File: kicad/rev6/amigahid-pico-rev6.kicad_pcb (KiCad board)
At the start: 2 copper layers, 100 x 80 mm, 115 parts, among them J1 A500 KBD OUT, J10 PS/2 KBD OUT, J11 DIN5 KBD IN, J12 PS/2 KBD IN, J13 USB-C AUX 5V, J2 DEBUG UART+SWD, J3 OLED I2C, J4 USB-A HOST, J7 SPARE GP28, J8 A500 KBD IN, J9 DIN5 KBD OUT, P1 DE9 MALE PORT 1, P2 DE9 MALE PORT 2, Q1 BSS138, Q10 BSS138, Q11 BSS138, Q12 BSS138, Q13 BSS138, Q14 BSS138, Q15 BSS138, Q16 BSS138, Q17 BSS138, Q18 BSS138, Q19 BSS138, Q2 BSS138, Q3 BSS138, Q4 BSS138, Q5 BSS138, Q6 BSS138, Q7 BSS138, Q8 BSS138, Q9 BSS138, U1 PicoW, U2 USBLC6-2SC6

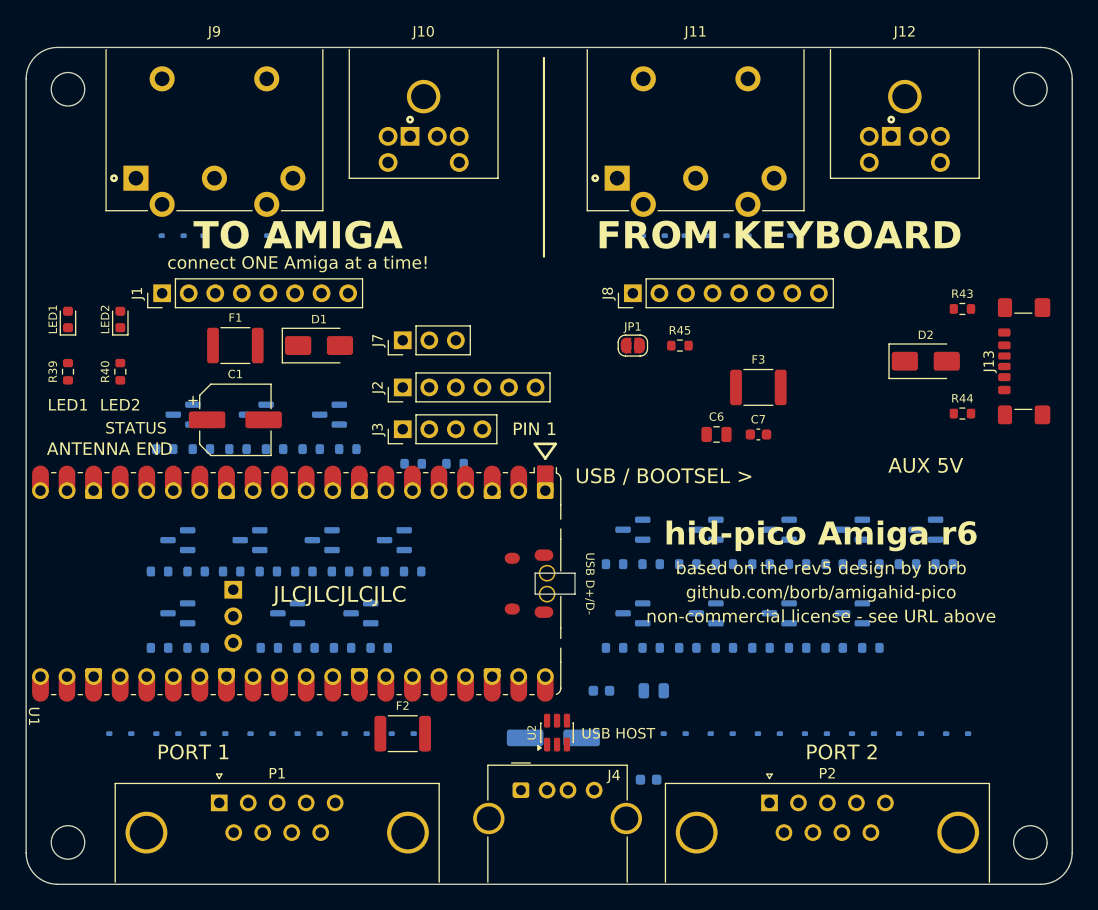
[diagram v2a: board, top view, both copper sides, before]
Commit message: kicad: route rev6 board
Copper for the whole board: 1524 track segments and 714 vias, 3.2 m of
copper, plus GND pours on both layers (69% / 68% coverage) with 400-odd
stitching vias on a 4 mm grid.  Power runs at 1.0 mm on its own netclass,
signals at 0.25 mm, +3V3 at 0.5 mm; the pours use thermal spokes on
through-hole pads and solid connections on SMD.

The shifter field had to be rearranged to make the board routable at all.
As drawn at M2 all four BSS138 groups sat between U1's two pad rows, and
the pull-ups lay flat at 1.6 mm pad pitch, which left 0.84-1.06 mm gaps -
about 0.4 mm of usable lane once clearance comes off, so almost nothing
could cross a pull-up row and the channels had to detour round the ends.
So:

  - every pull-up stands on end (90 deg), which cuts its width across the
    row from 2.4 mm to 0.95 mm and opens the gaps to ~2.5 mm.  All of
    them face the same way, channel pad toward its FET, rail pad away,
    so the SYS5V rail no longer runs along a row of channel pads.
  - each FET row moved 0.8-1.3 mm off its pull-ups, turning 0.63 mm dead
    lanes into 1.4-1.9 mm ones.
  - the b1/b2/b3 groups of both ports moved south of the module, into the
    band that only held the ESD clamps, next to the connector pins they
    serve.  The clamps moved south to make room.
  - U2 turned 180 deg: its VBUS pin was boxed in between the two USB data
    pins with 0.35 mm either side and a ground pad due south.

The USB pair is laid by hand.  Both taps sit on the edge of the milled
window, so each run starts 0.43 mm clear of it inside its castellated
pad; usb_dp goes west round the window and threads the 0.94 mm gap
between U1's bottom castellations 39 and 40, usb_dm runs down the east
side with a 1.5 mm jog to match length.  24.4 mm and 20.7 mm, 3.7 mm
apart.  J13's USB-C VBUS pins are hand laid too: 0.29 mm of gap to the
CC pads means they leave on a 0.6 mm neck before widening.

tools/check_rev6_pcb.py: all 31 assertions pass.
tools/check_rev6_netlist.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
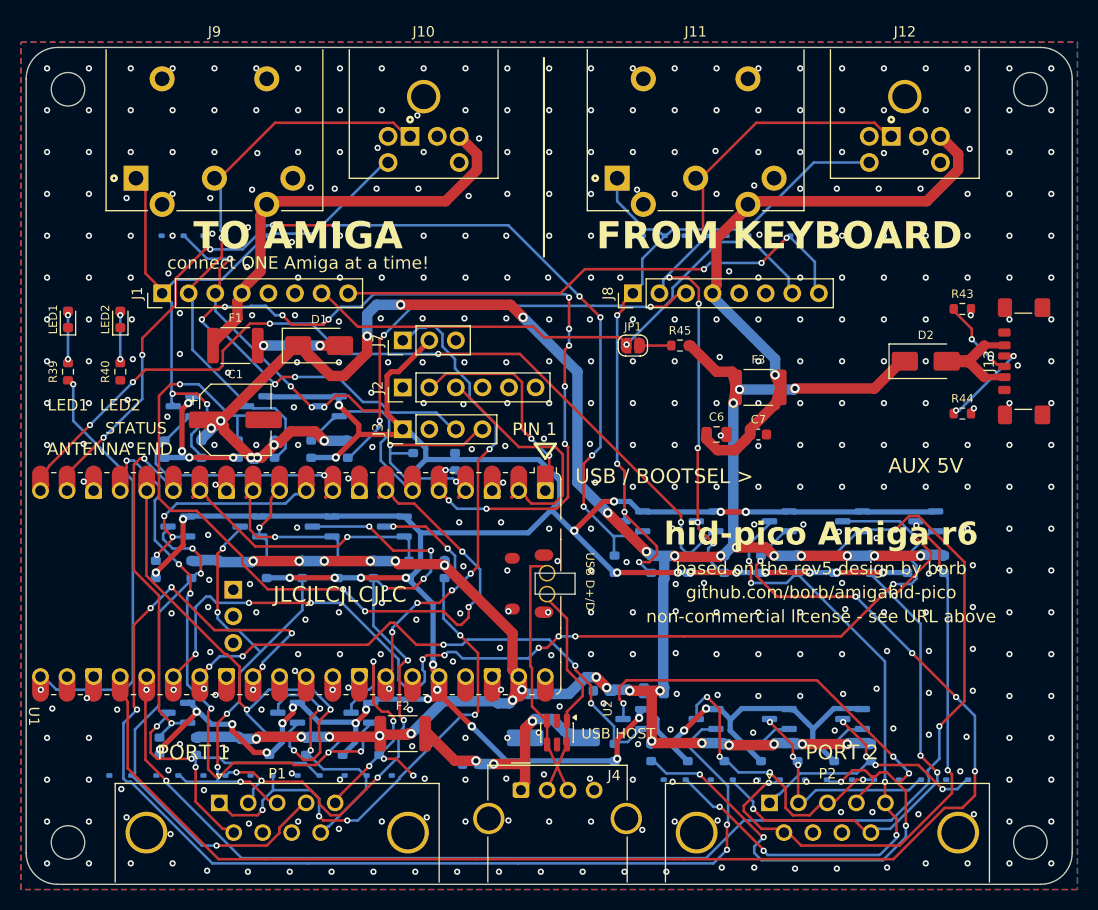
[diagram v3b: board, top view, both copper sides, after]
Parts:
- moved C5 17.1 mm to (42.5, 68.5)
- moved Q16 10.1 mm to (58.0, 64.2)
- moved Q17 10.1 mm to (65.0, 64.2)
- moved Q18 10.1 mm to (72.0, 64.2)
- moved Q19 10.1 mm to (79.0, 64.2)
- moved R31 10.0 mm to (56.2, 67.4), turned to 90 degrees
- moved R32 10.0 mm to (59.8, 67.4), turned to -90 degrees
- moved R33 10.0 mm to (63.2, 67.4), turned to 90 degrees
- moved R34 10.0 mm to (66.8, 67.4), turned to -90 degrees
- moved R35 10.0 mm to (70.2, 67.4), turned to 90 degrees
- moved R36 10.0 mm to (73.8, 67.4), turned to -90 degrees
- moved R37 10.0 mm to (77.2, 67.4), turned to 90 degrees
- moved R38 10.0 mm to (80.8, 67.4), turned to -90 degrees
- moved Q10 9.50 mm to (32.0, 63.6)
- moved Q8 9.50 mm to (14.5, 63.6)
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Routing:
- net +3V3: track 0.00 -> 321.5 mm, vias 0 -> 40
- net /SYS5V: track 0.00 -> 283.2 mm, vias 0 -> 45
- net /cont2_b3_lo: track 0.00 -> 135.1 mm, vias 0 -> 5
- net /cont2_b2_lo: track 0.00 -> 130.0 mm, vias 0 -> 4
- net /cont2_vq_lo: track 0.00 -> 118.4 mm, vias 0 -> 8
- net /i2c_scl: track 0.00 -> 104.0 mm, vias 0 -> 14
- net /kbin_clk_lo: track 0.00 -> 98.8 mm, vias 0 -> 9
- net /cont2_b1_lo: track 0.00 -> 96.1 mm, vias 0 -> 10
- net /kbin_dat_lo: track 0.00 -> 85.7 mm, vias 0 -> 5
- net /cont2_hq: track 0.00 -> 84.5 mm, vias 0 -> 7
- net /kbdata_lo: track 0.00 -> 79.7 mm, vias 0 -> 5
- net /kbreset: track 0.00 -> 75.2 mm, vias 0 -> 7
- net /kbin_clk: track 0.00 -> 68.6 mm, vias 0 -> 4
- net /kbin_dat: track 0.00 -> 67.1 mm, vias 0 -> 6
- net /cont2_b3: track 0.00 -> 64.7 mm, vias 0 -> 6
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- added copper zone on B.Cu, net GND
- added copper zone on F.Cu, net GND

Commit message: kicad: finish the rev6 copper
Pours re-laid with a 2.5 mm stitching grid (1028 ground vias, 69.3% /
68.8% coverage), thermal relief tightened to 0.15 mm gap / 0.4 mm spokes
so the through-hole ground pads keep two spokes, and the rail vias taken
down to 0.6/0.3 - at 0.8/0.4 a handful sat 0.475 mm from a 0603 pad's
copper where the copper-to-hole rule wants 0.5 mm.

The USB pair is re-laid to swap sides on the back layer just in front of
J4: U2 puts usb_dp on the west column and J4 on the east, so the pair has
to cross once, and doing it under the board keeps both runs clear of each
other.  usb_dp 24.7 mm, usb_dm 22.8 mm.

DRC is down to 2 starved thermals and 12 unconnected items; the detail is
in the commit thread.  Netlist checker 356/356, pcb checker 31/31.
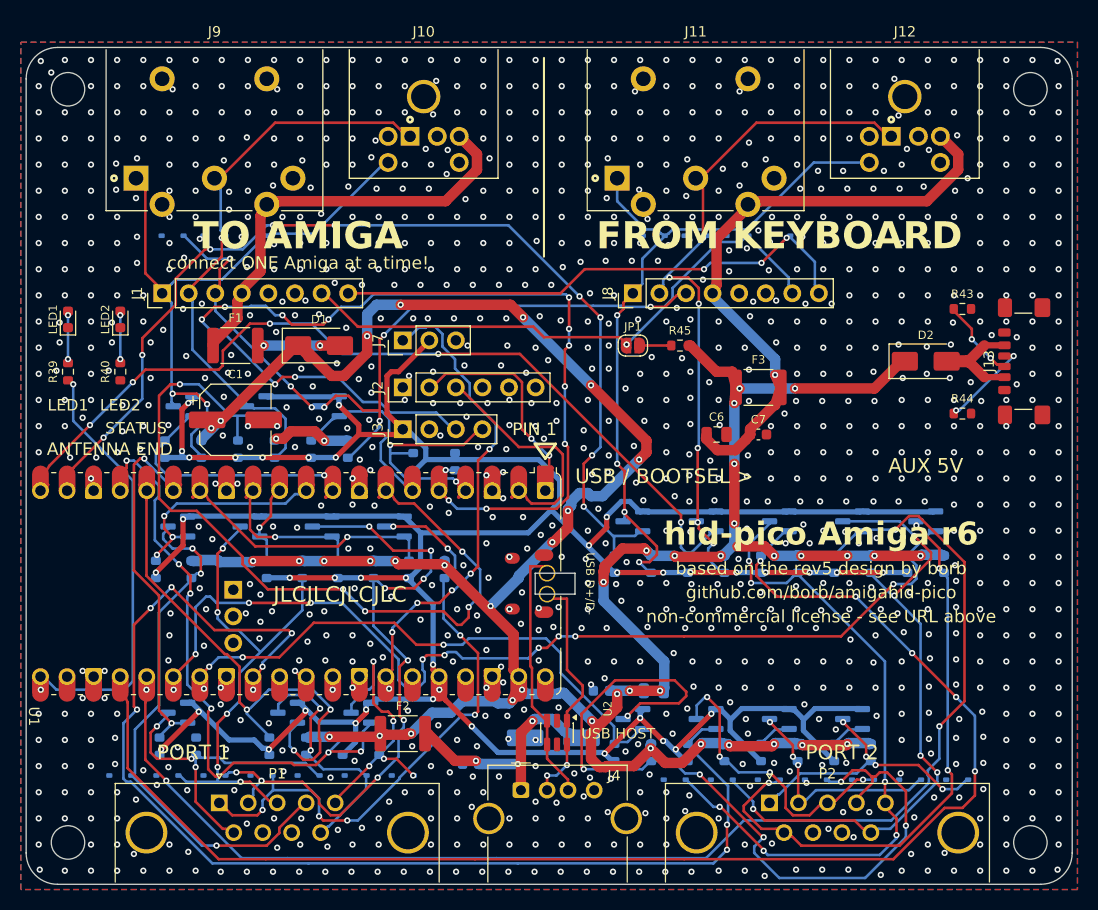
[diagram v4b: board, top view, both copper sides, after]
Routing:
- net /SYS5V: track 283.2 -> 292.5 mm, vias 45 -> 48
- net +3V3: track 321.5 -> 325.9 mm, vias 40 -> 39
- net /cont2_hq: track 84.5 -> 80.8 mm, vias 7 -> 6
- net /usb_dm: track 20.7 -> 22.8 mm, vias 0 -> 2
- net /cont2_hq_lo: vias 6 -> 4
- net GND: vias 426 -> 1028

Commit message: kicad: rf board keep-out, shifter designators and jlc-legal silk
Layout review fixes that touch no signal copper.  DRC is unchanged by this
commit: still the same 2 starved thermals on U1 pad 28 and the same 12
unconnected items, and no new violation of any other kind.

Outline
  - Cut the west edge back to x = 8.5 mm between y = 43.71 and 58.81 with R1
    inner fillets.  Raspberry Pi's own Pico W footprint carries a "Board Keep
    Out Suggestion RF" rectangle on Edge.Cuts reaching 8.5 mm inboard of the
    antenna end: the carrier is meant to be cut away under the antenna, not
    merely kept free of copper, and the board only overhung it by 1 mm.  The
    strip lies between the module's two pad rows and inside the antenna
    keep-out, so it was already empty - nothing was moved to make room, both
    pad rows keep full support, and copper-to-edge is unaffected.
  - Dropped 9 GND stitching vias that sat 0.31-0.42 mm from the M3 holes.
    Those holes are Edge.Cuts cutouts, so they are milled with profile
    tolerance rather than drilled; 0.3 mm is inside JLC's rule but is not much
    to hand a router bit, and these are redundant vias in a pour.

Connectors
  - Mini-DIN SH hole 2.40 -> 2.50 mm, in the footprint and both instances.
    2.40 leaves the Kycon KMDGX alternate's 2.30 mm locating boss only 0.10 mm
    diametral slack, which becomes a press fit once plating and hole tolerance
    come off; the Same Sky flat earth tab does not care.  The 3.20 mm pad still
    keeps a 0.35 mm ring.  Three stitching vias moved out of the way to hold
    the 0.5 mm hole-to-hole spacing.

Silkscreen
  - Turned on and placed all 78 hidden designators: Q1-Q19, R1-R38 and
    D10-D30, i.e. the whole bottom-side shifter and clamp field, which printed
    as an anonymous grid of SOT-23s and 0603s.  Bring-up probes those channels
    and the rework path is hand-soldering.
  - J9/J10/J11/J12 printed their designators at y = -1.5 mm, entirely off the
    board; they now sit in the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
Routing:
- net GND: track 0.00 -> 4.50 mm, vias 1028 -> 1021
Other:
- outline, holes or cut-outs redrawn

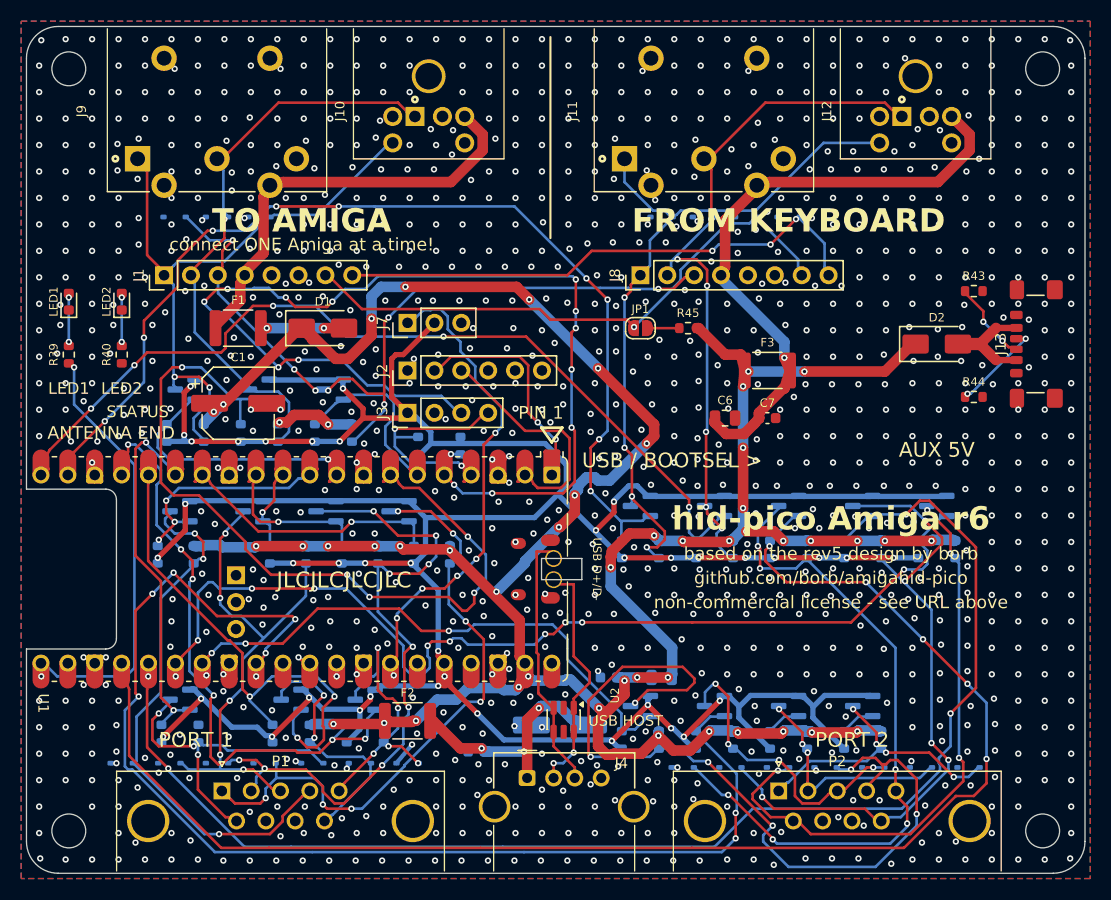
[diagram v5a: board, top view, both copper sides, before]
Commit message: kicad: thin the rev6 stitching via field
the board carried 1021 ground stitching vias on a 2.5 mm grid.  with
min_hole_clearance at 0.5 mm that is a pegboard: every corridor a signal needs is
fenced off by via holes, which is why eight nets were still open and four ESD clamps
were sitting on pour islands of their own.

the layout plan only asks for a tie about every 10 mm in open regions and the checker
only wants fifteen, so the field goes.  what is left are the vias that carry a stub -
clamp anchors and island ties - and the ties the stitcher then adds to keep the plane
one electrical island.  1021 vias down to 25.

no net changes: the same twelve items are unconnected before and after.
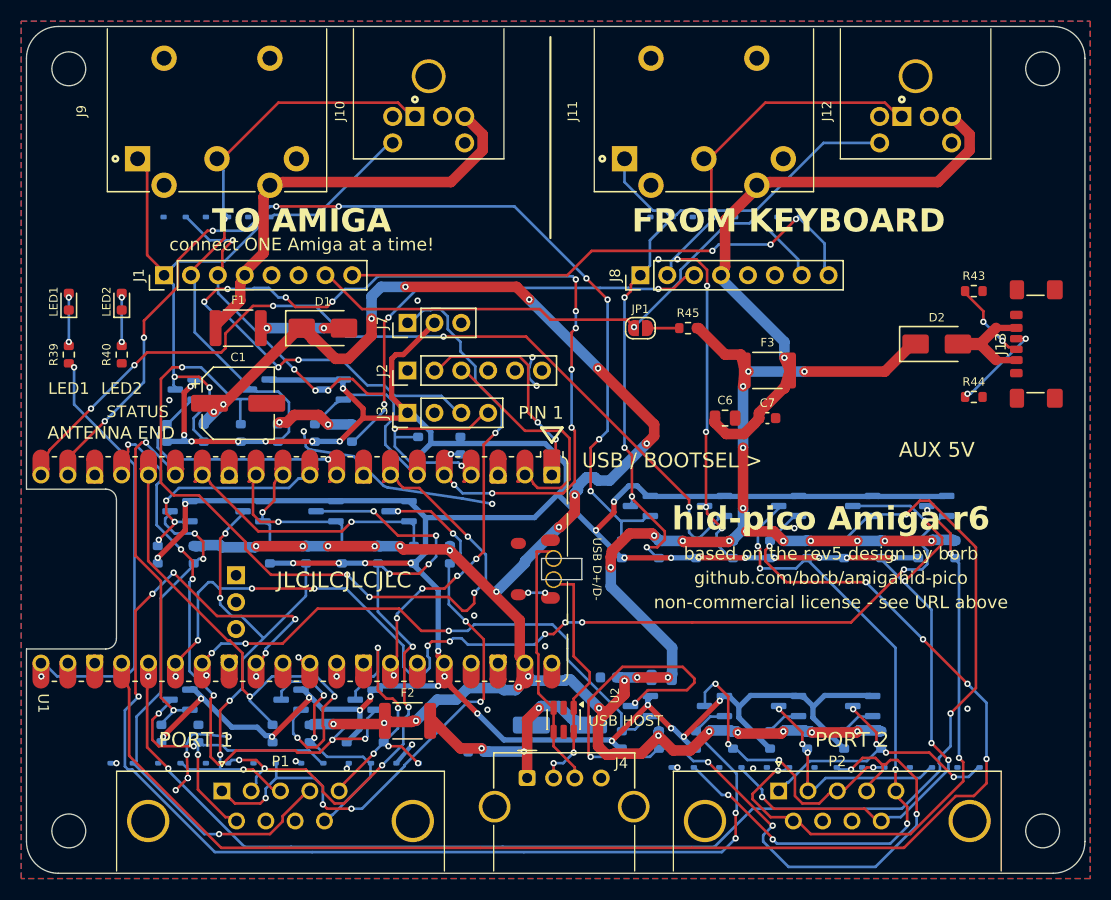
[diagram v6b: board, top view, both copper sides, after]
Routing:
- net GND: track 4.50 -> 39.0 mm, vias 1021 -> 25
